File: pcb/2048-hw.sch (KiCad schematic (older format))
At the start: 98 parts, among them J1 UJC-HP-3-SMT-TR, J2 Battery, J3 SWD, SW1 SW_SPDT, SW2 PUSH_A, SW3 PUSH_B, U1 STM32F303K8Tx, U2 MCP73831-2-OT, U3 AP2210N-3.3TRG1, U4 PSP_1000_JSTK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

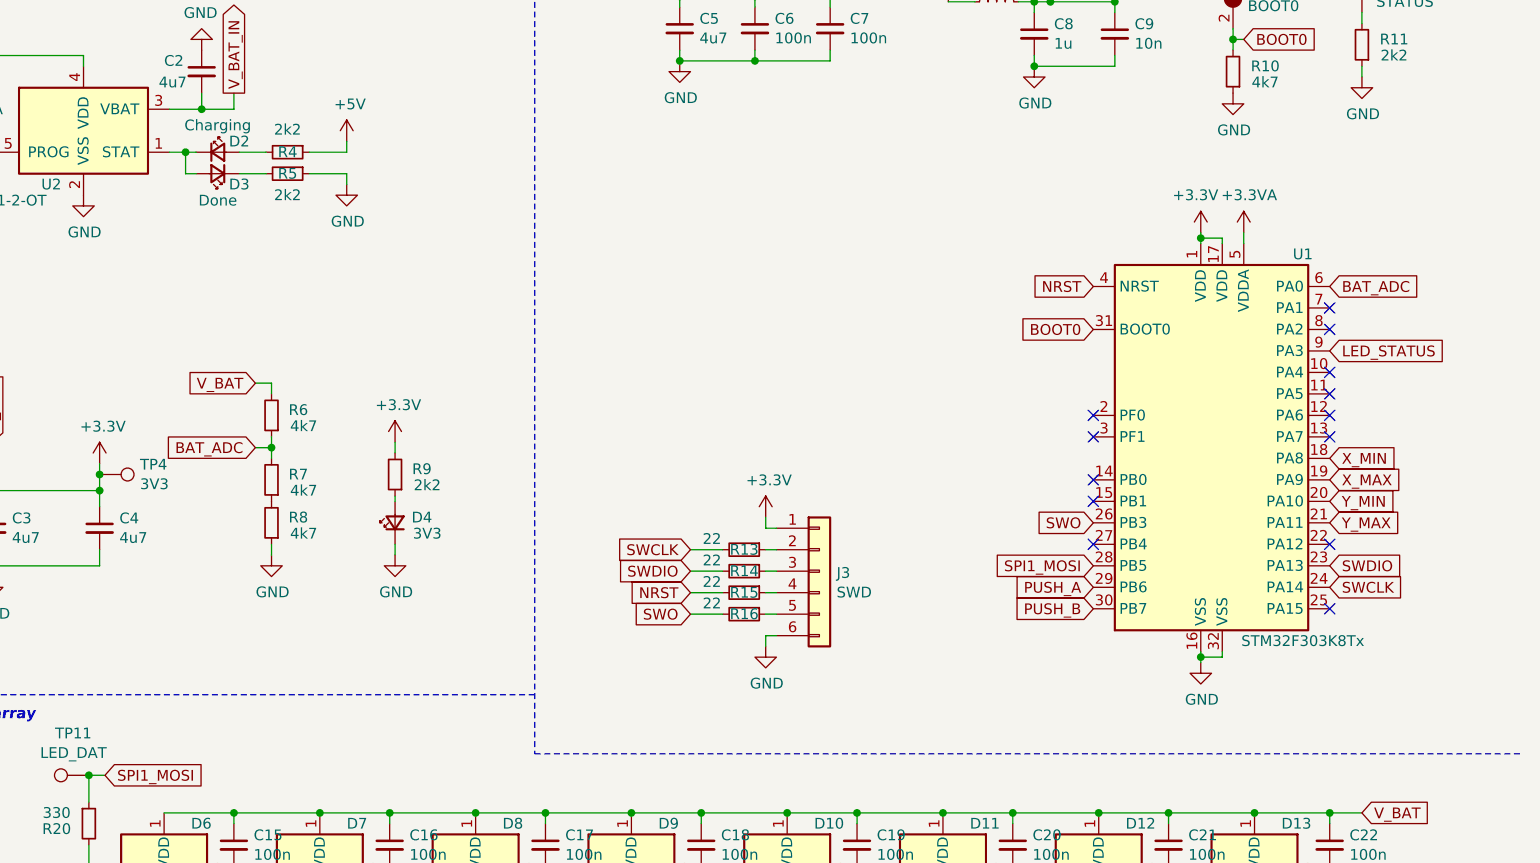
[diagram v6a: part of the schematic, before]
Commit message: pcb: Add AT24C08D EEPROM to schematic
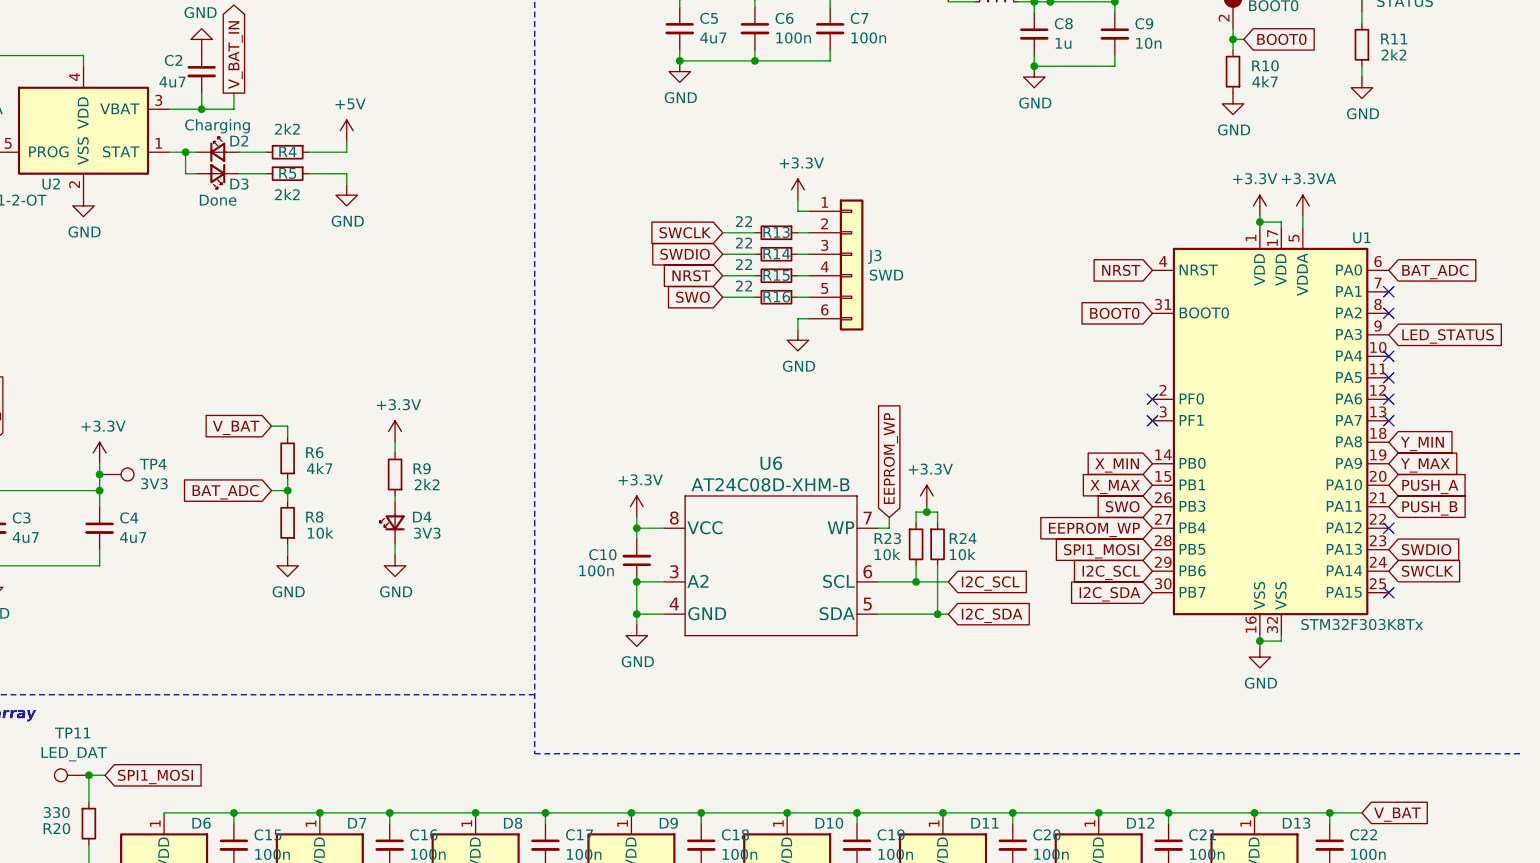
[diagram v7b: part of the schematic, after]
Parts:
- removed R7: 4k7, Resistor_SMD:R_0603_1608Metric_Pad0.98x0.95mm_HandSolder, symbol Device:R_Small
- added C10: 100n, Capacitor_SMD:C_0603_1608Metric_Pad1.08x0.95mm_HandSolder, symbol Device:C_Small
- added R23, R24: 10k, Resistor_SMD:R_0603_1608Metric_Pad0.98x0.95mm_HandSolder, symbol Device:R_Small
- added U6: AT24C08D-XHM-B, Package_SO:TSSOP-8_4.4x3mm_P0.65mm, symbol 2048-hw:AT24C08D-XHM-B
- R8: value 4k7 -> 10k
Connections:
- net +3V3: now also C10.2, R23.1, R24.1, U6.8 (VCC)
- net BAT_ADC: now also R8.2
- net GND: now also C10.1, U6.3 (A2), U6.4 (GND)
- net PUSH_A: now also U1.20 (PA10); no longer U1.29 (PB6)
- net PUSH_B: now also U1.21 (PA11); no longer U1.30 (PB7)
- net X_MAX: now also U1.15 (PB1); no longer U1.19 (PA9)
- net X_MIN: now also U1.14 (PB0); no longer U1.18 (PA8)
- net Y_MAX: now also U1.19 (PA9); no longer U1.21 (PA11)
- net Y_MIN: now also U1.18 (PA8); no longer U1.20 (PA10)
- net EEPROM_WP: now reaches U1.27 (PB4)
- net EEPROM_WP: now also U6.7 (WP)
- new net I2C_SCL: R23.2, U1.29 (PB6), U6.6 (SCL)
- new net I2C_SDA: R24.2, U1.30 (PB7), U6.5 (SDA)
- no-connect marks 15 -> 12
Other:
- moved on the sheet: J3, R13, R14, R15, R16, R6, R8, U1

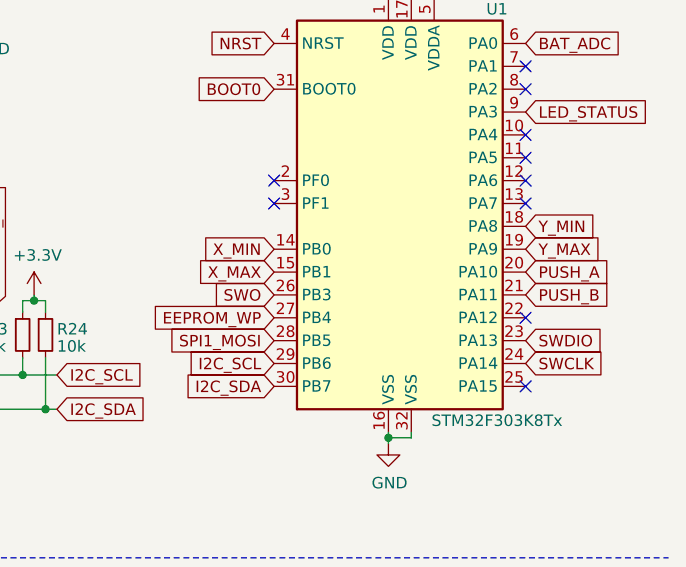
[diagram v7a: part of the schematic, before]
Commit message: pcb: Make routing changes to facilitate EEPROM
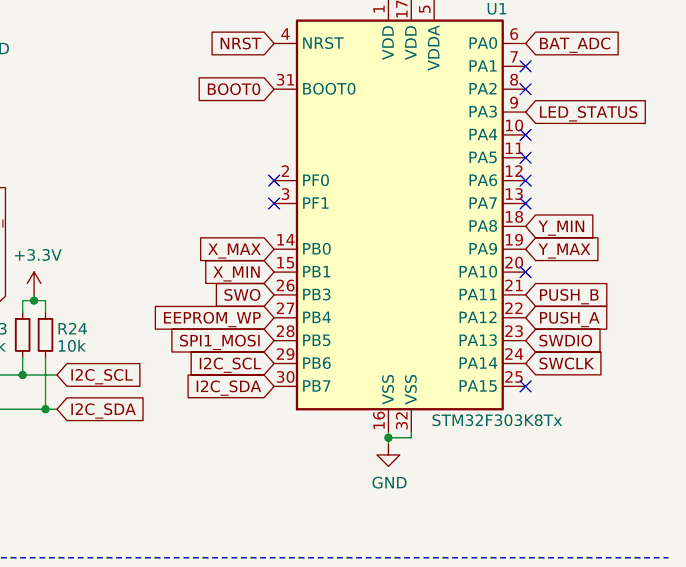
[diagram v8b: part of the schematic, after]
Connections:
- net PUSH_A: now also U1.22 (PA12); no longer U1.20 (PA10)
- net X_MAX: now also U1.14 (PB0); no longer U1.15 (PB1)
- net X_MIN: now also U1.15 (PB1); no longer U1.14 (PB0)
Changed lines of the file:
@@
 Text GLabel 10600 3150 2    50   Input ~ 0
 Y_MIN
+Text GLabel 9500 3250 0    50   Input ~ 0
+X_MAX
 Text GLabel 9500 3350 0    50   Input ~ 0
-X_MAX
-Text GLabel 9500 3250 0    50   Input ~ 0
 X_MIN
 Wire Wire Line
@@
 	0    -1   -1   0
 $EndComp
-NoConn ~ 10600 3550
+NoConn ~ 10600 3350
 NoConn ~ 10600 2750
 NoConn ~ 10600 2550
@@
 Wire Wire Line
 	1625 6225 1625 6250
-Text GLabel 10600 3350 2    50   Input ~ 0
+Text GLabel 10600 3550 2    50   Input ~ 0
 PUSH_A
 Text GLabel 10600 3450 2    50   Input ~ 0
